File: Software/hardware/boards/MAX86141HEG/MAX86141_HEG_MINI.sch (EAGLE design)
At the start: 18 parts, among them U1 MAX86141ENP+T, U3 TXBN0304RUTR, U4 LP5907MFX-3.3/NOPB

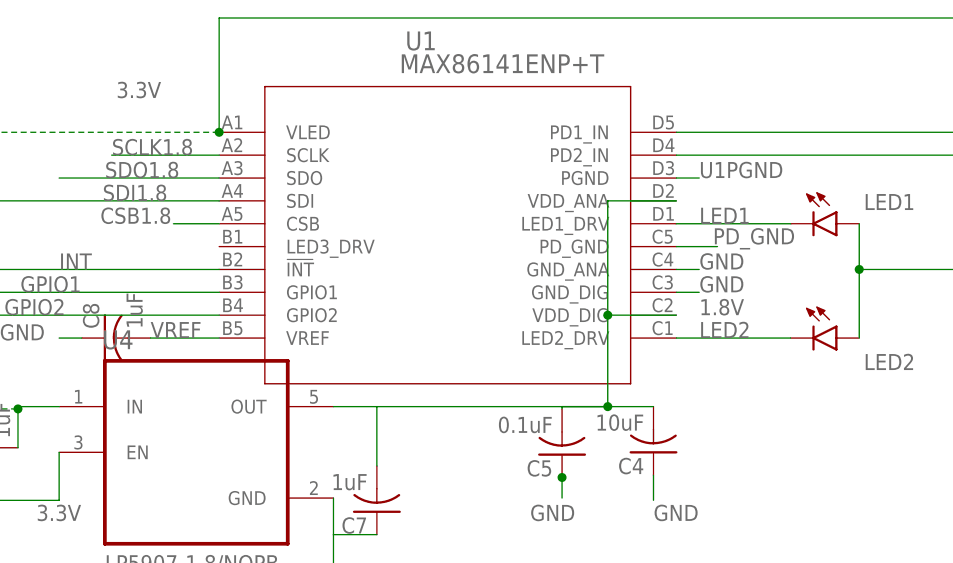
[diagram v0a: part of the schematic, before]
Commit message: lolin32 firmware should update properly now
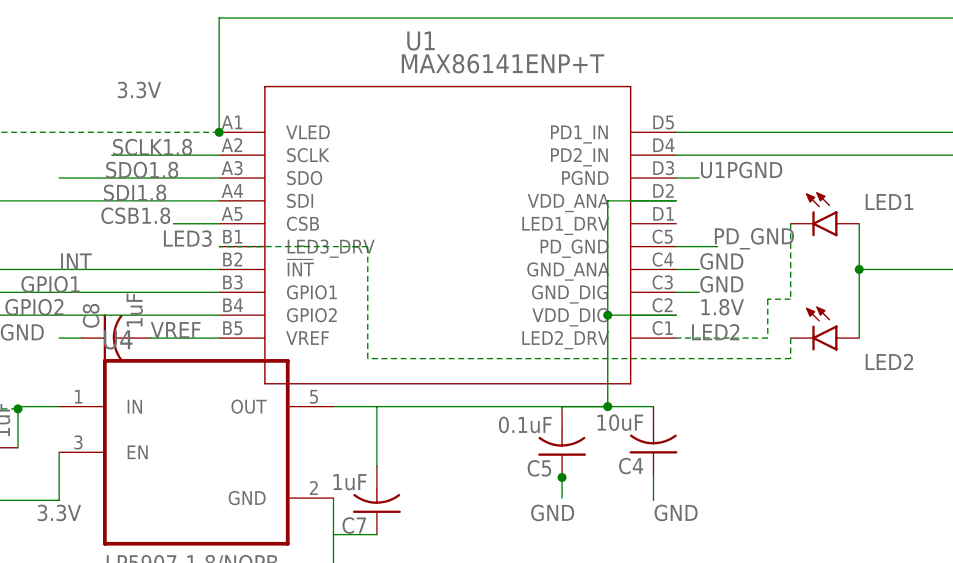
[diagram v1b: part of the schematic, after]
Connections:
- removed net LED1: LED1.C, U1.LED1_DRV
- new net LED3: LED2.C, U1.LED3_DRV
- net LED2: now also LED1.C; no longer LED2.C
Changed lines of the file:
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@@
 </busses>
 <nets>
-<net name="LED2" class="0">
-<segment>
-<pinref part="U1" gate="A" pin="LED2_DRV"/>
-<pinref part="LED2" gate="G$1" pin="C"/>
-<wire x1="96.52" y1="73.66" x2="109.22" y2="73.66" width="0.1524" layer="91"/>
-<label x="99.06" y="73.66" size="1.778" layer="95"/>
-</segment>
-</net>
-<net name="LED1" class="0">
-<segment>
-<pinref part="U1" gate="A" pin="LED1_DRV"/>
-<pinref part="LED1" gate="G$1" pin="C"/>
-<wire x1="96.52" y1="86.36" x2="109.22" y2="86.36" width="0.1524" layer="91"/>
-<label x="99.06" y="86.36" size="1.778" layer="95"/>
-</segment>
-</net>
 <net name="VREF" class="0">
 <segment>
@@
 </segment>
 </net>
+<net name="LED3" class="0">
+<segment>
+<pinref part="LED2" gate="G$1" pin="C"/>
+<wire x1="109.22" y1="73.66" x2="109.22" y2="71.374" width="0.1524" layer="91" style="longdash"/>
+<wire x1="109.22" y1="71.374" x2="62.23" y2="71.374" width="0.1524" layer="91" style="longdash"/>
+<wire x1="62.23" y1="71.374" x2="62.23" y2="83.82" width="0.1524" layer="91" style="longdash"/>
+<pinref part="U1" gate="A" pin="LED3_DRV"/>
+<wire x1="62.23" y1="83.82" x2="45.72" y2="83.82" width="0.1524" layer="91" style="longdash"/>
+<label x="39.37" y="83.82" size="1.778" layer="95"/>
+</segment>
+</net>
+<net name="LED2" class="0">
+<segment>
+<pinref part="LED1" gate="G$1" pin="C"/>
+<wire x1="109.22" y1="86.36" x2="109.22" y2="77.978" width="0.1524" layer="91" style="longdash"/>
+<wire x1="109.22" y1="77.978" x2="106.68" y2="77.978" width="0.1524" layer="91" style="longdash"/>
+<pinref part="U1" gate="A" pin="LED2_DRV"/>
+<wire x1="106.68" y1="77.978" x2="106.68" y2="73.66" width="0.1524" layer="91" style="longdash"/>
+<wire x1="106.68" y1="73.66" x2="96.52" y2="73.66" width="0.1524" layer="91" style="longdash"/>
+<label x="98.044" y="73.406" size="1.778" layer="95"/>
+</segment>
+</net>
